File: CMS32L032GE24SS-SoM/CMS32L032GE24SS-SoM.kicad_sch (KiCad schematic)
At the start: 3 parts, among them J105 Connection to DAPLink Board

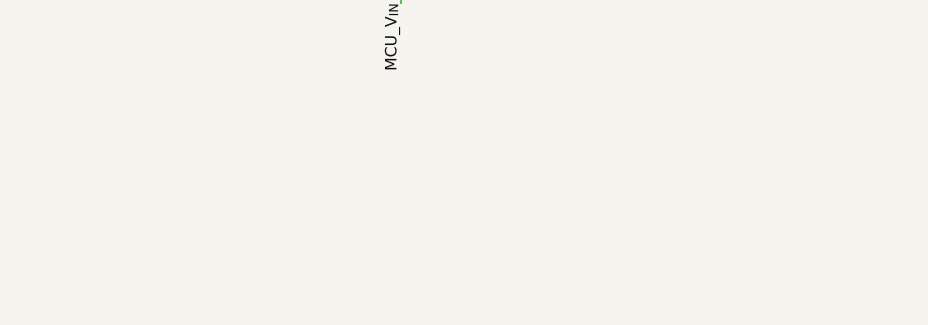
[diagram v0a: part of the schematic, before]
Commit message: basic layout of chips
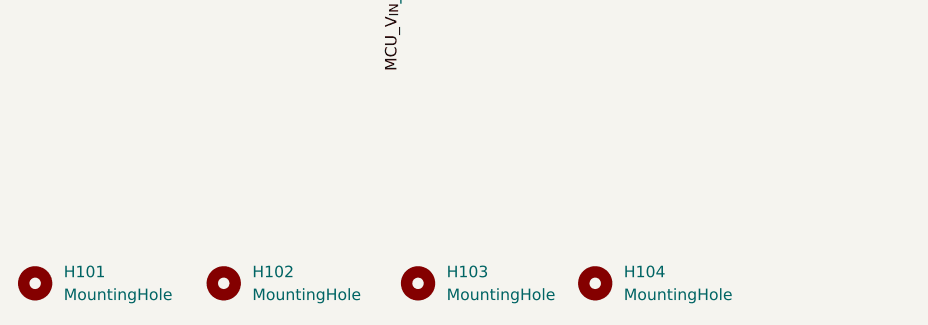
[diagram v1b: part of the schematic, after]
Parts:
- added H101, H102, H103, H104: MountingHole, IotPi_MountingHoles:MountingHole_1.8mm, symbol Mechanical:MountingHole
- J105: footprint (none) -> Connector_PinHeader_1.27mm:PinHeader_1x08_P1.27mm_Horizontal
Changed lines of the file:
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@@
     (effects (font (size 1.27 1.27)) (justify right bottom))
+  )
+  (symbol (lib_id "Mechanical:MountingHole") (at 86.995 183.515 0) (unit 1)
+    (in_bom no) (on_board yes) (dnp no) (fields_autoplaced)
+    (property "Reference" "H104" (at 90.17 182.245 0)
+      (effects (font (size 1.27 1.27)) (justify left))
+    )
+    (property "Value" "MountingHole" (at 90.17 184.785 0)
+      (effects (font (size 1.27 1.27)) (justify left))
+    )
+    (property "Footprint" "IotPi_MountingHoles:MountingHole_1.8mm" (at 86.995 183.515 0)
+      (effects (font (size 1.27 1.27)) hide)
+    )
+    (property "Datasheet" "~" (at 86.995 183.515 0)
+      (effects (font (size 1.27 1.27)) hide)
+    )
+    (instances
+      (project "CMS32L032GE24SS-SoM"
+        (path "/c0ebcd8e-c90a-40d9-842d-ee55e79d6adf"
+          (reference "H104") (unit 1)
+        )
+      )
+    )
+  )
+  (symbol (lib_id "Mechanical:MountingHole") (at 67.31 183.515 0) (unit 1)
+    (in_bom no) (on_board yes) (dnp no) (fields_autoplaced)
+    (property "Reference" "H103" (at 70.485 182.245 0)
+      (effects (font (size 1.27 1.27)) (justify left))
+    )
+    (property "Value" "MountingHole" (at 70.485 184.785 0)
+      (effects (font (size 1.27 1.27)) (justify left))
+    )
+    (property "Footprint" "IotPi_MountingHoles:MountingHole_1.8mm" (at 67.31 183.515 0)
+      (effects (font (size 1.27 1.27)) hide)
+    )
+    (property "Datasheet" "~" (at 67.31 183.515 0)
+      (effects (font (size 1.27 1.27)) hide)
+    )
+    (instances
+      (project "CMS32L032GE24SS-SoM"
+        (path "/c0ebcd8e-c90a-40d9-842d-ee55e79d6adf"
+          (reference "H103") (unit 1)
+        )
+      )
+    )
+  )
+  (symbol (lib_id "Mechanical:MountingHole") (at 24.765 183.515 0) (unit 1)
+    (in_bom no) (on_board yes) (dnp no) (fields_autoplaced)
+    (property "Reference" "H101" (at 27.94 182.245 0)
+      (effects (font (size 1.27 1.27)) (justify left))
+    )
+    (property "Value" "MountingHole" (at 27.94 184.785 0)
+      (effects (font (size 1.27 1.27)) (justify left))
+    )
+    (property "Footprint" "IotPi_MountingHoles:MountingHole_1.8mm" (at 24.765 183.515 0)
+      (effects (font (size 1.27 1.27)) hide)
+    )
+    (property "Datasheet" "~" (at 24.765 183.515 0)
+      (effects (font (size 1.27 1.27)) hide)
+    )
+    (instances
+      (project "CMS32L032GE24SS-SoM"
+        (path "/c0ebcd8e-c90a-40d9-842d-ee55e79d6adf"
+          (reference "H101") (unit 1)
+        )
+      )
+    )
   )
   (symbol (lib_id "power:PWR_FLAG") (at 83.82 110.49 0) (unit 1)
@@
         (path "/c0ebcd8e-c90a-40d9-842d-ee55e79d6adf"
           (reference "#PWR0103") (unit 1)
+        )
+      )
+    )
+  )
+  (symbol (lib_id "Mechanical:MountingHole") (at 45.72 183.515 0) (unit 1)
+    (in_bom no) (on_board yes) (dnp no) (fields_autoplaced)
+    (property "Reference" "H102" (at 48.895 182.245 0)
+      (effects (font (size 1.27 1.27)) (justify left))
+    )
+    (property "Value" "MountingHole" (at 48.895 184.785 0)
+      (effects (font (size 1.27 1.27)) (justify left))
+    )
+    (property "Footprint" "IotPi_MountingHoles:MountingHole_1.8mm" (at 45.72 183.515 0)
+      (effects (font (size 1.27 1.27)) hide)
+    )
+    (property "Datasheet" "~" (at 45.72 183.515 0)
+      (effects (font (size 1.27 1.27)) hide)
+    )
+    (instances
+      (project "CMS32L032GE24SS-SoM"
+        (path "/c0ebcd8e-c90a-40d9-842d-ee55e79d6adf"
+          (reference "H102") (unit 1)
         )
       )
@@
       (effects (font (size 1.27 1.27)))
     )
-    (property "Footprint" "" (at 41.91 34.925 0)
-      (effects (font (size 1.27 1.27)) hide)
-    )
+    (property "Footprint" "Connector_PinHeader_1.27mm:PinHeader_1x08_P1.27mm_Horizontal" (at 41.91 34.925 0)
+      (effects (font (size 1.27 1.27)) hide)
+    )

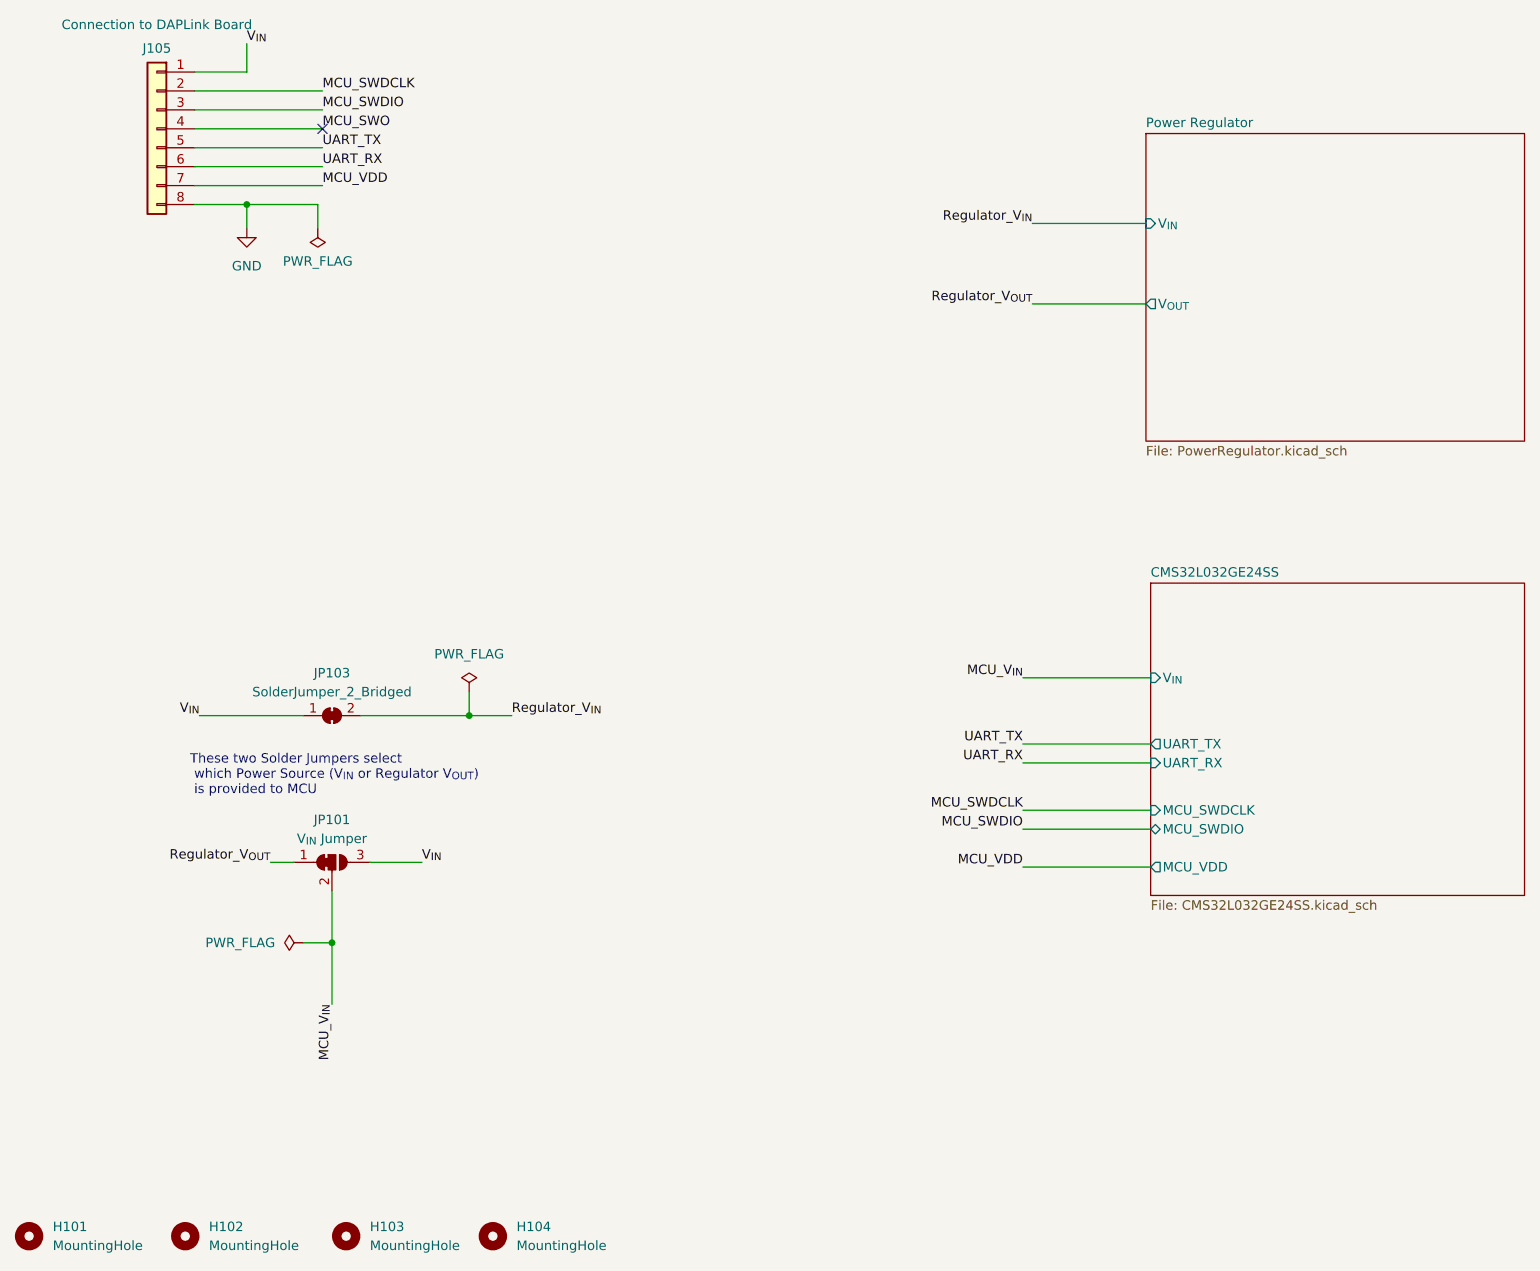
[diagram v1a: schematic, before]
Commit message: locked ArduinoNano board
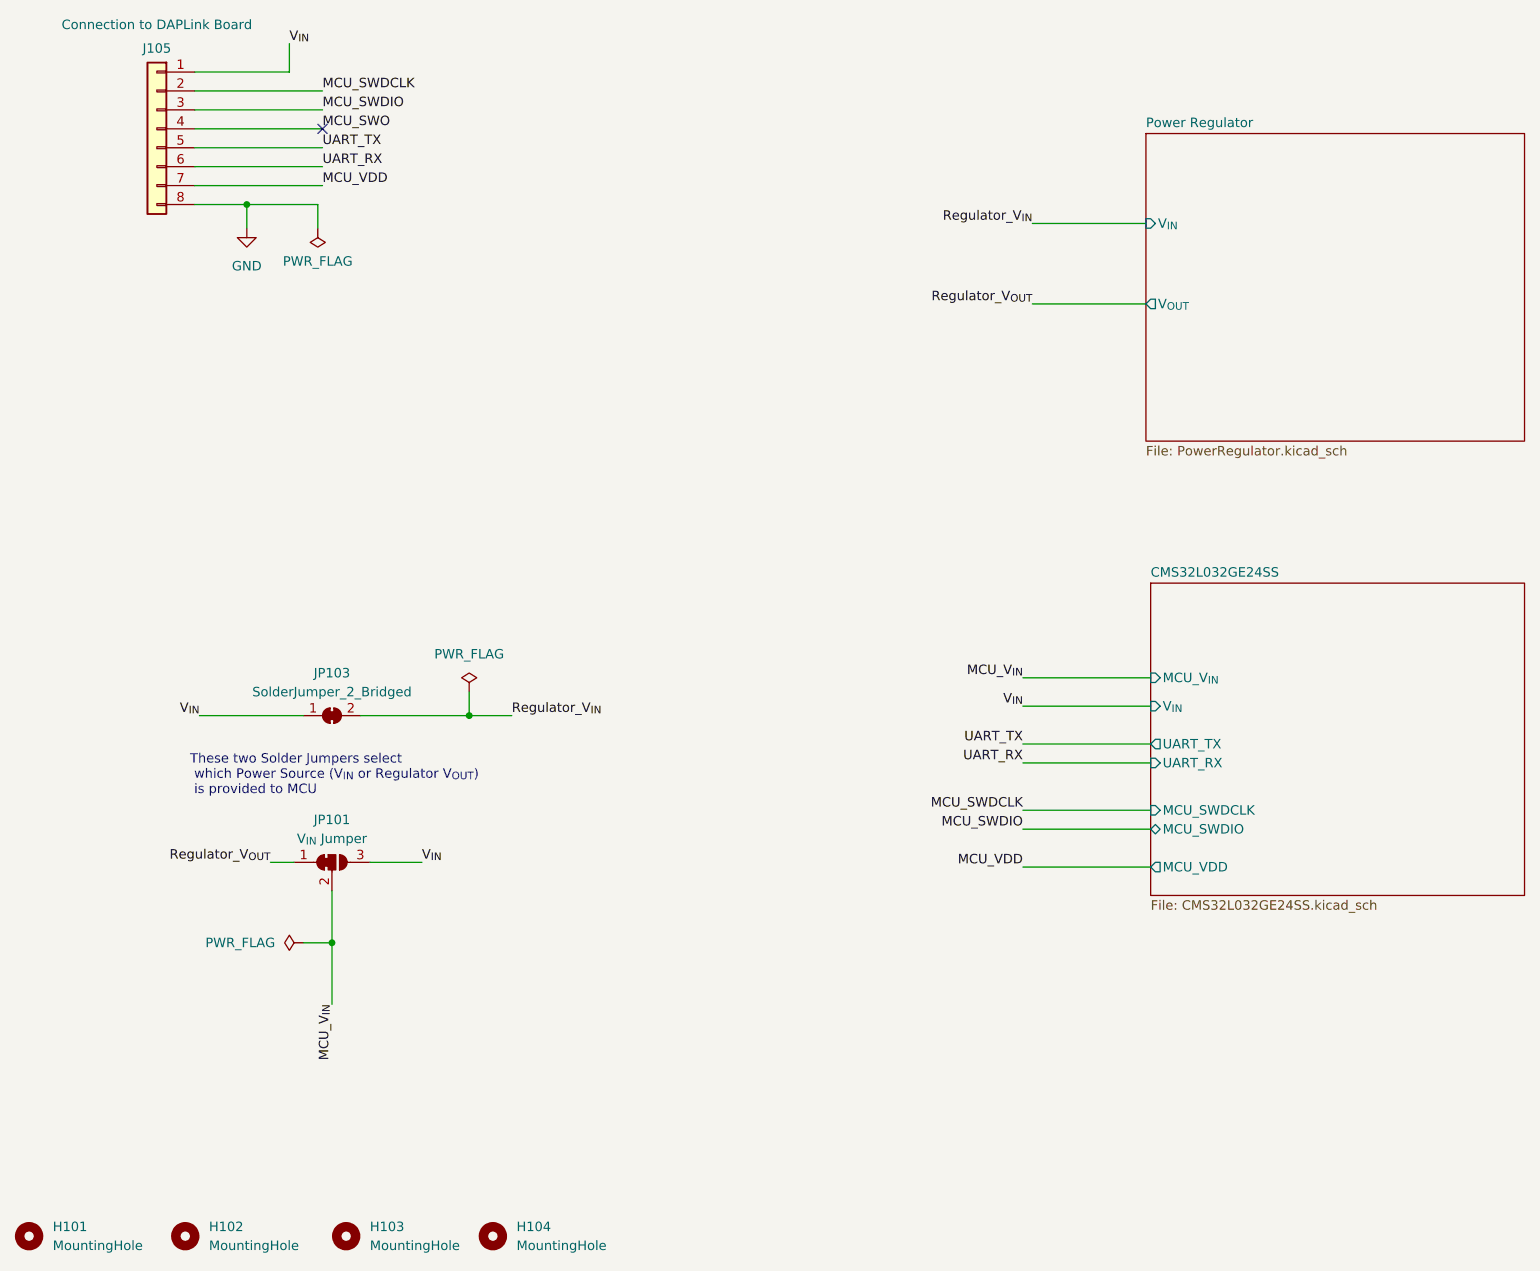
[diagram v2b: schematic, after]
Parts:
- H101, H102, H103, H104: footprint IotPi_MountingHoles:MountingHole_1.8mm -> IotPi_ArduinoNanoMountingHoles:ArduinoNano_MountingHole
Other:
- sheet CMS32L032GE24SS ports: added MCU_V_{IN}; removed none
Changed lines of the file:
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@@
     (stroke (width 0) (type default))
   )
-  (wire (pts (xy 53.975 27.305) (xy 46.99 27.305))
+  (wire (pts (xy 59.69 27.305) (xy 46.99 27.305))
     (stroke (width 0) (type default))
   )
@@
     (stroke (width 0) (type default))
   )
+  (wire (pts (xy 158.115 112.395) (xy 175.26 112.395))
+    (stroke (width 0) (type default))
+  )
   (wire (pts (xy 158.115 108.585) (xy 175.26 108.585))
     (stroke (width 0) (type default))
   )
-  (wire (pts (xy 53.975 23.495) (xy 53.975 27.305))
+  (wire (pts (xy 59.69 23.495) (xy 59.69 27.305))
     (stroke (width 0) (type default))
   )
@@
     (effects (font (size 1.27 1.27)) (justify left bottom))
   )
-  (label "V_{IN}" (at 53.975 23.495 0) (fields_autoplaced)
+  (label "V_{IN}" (at 59.69 23.495 0) (fields_autoplaced)
     (effects (font (size 1.27 1.27)) (justify left bottom))
   )
@@
   )
   (label "Regulator_V_{OUT}" (at 57.15 133.35 180) (fields_autoplaced)
+    (effects (font (size 1.27 1.27)) (justify right bottom))
+  )
+  (label "V_{IN}" (at 158.115 112.395 180) (fields_autoplaced)
     (effects (font (size 1.27 1.27)) (justify right bottom))
   )
@@
       (effects (font (size 1.27 1.27)) (justify left))
     )
-    (property "Footprint" "IotPi_MountingHoles:MountingHole_1.8mm" (at 86.995 183.515 0)
+    (property "Footprint" "IotPi_ArduinoNanoMountingHoles:ArduinoNano_MountingHole" (at 86.995 183.515 0)
       (effects (font (size 1.27 1.27)) hide)
     )
@@
       (effects (font (size 1.27 1.27)) (justify left))
     )
-    (property "Footprint" "IotPi_MountingHoles:MountingHole_1.8mm" (at 67.31 183.515 0)
+    (property "Footprint" "IotPi_ArduinoNanoMountingHoles:ArduinoNano_MountingHole" (at 67.31 183.515 0)
       (effects (font (size 1.27 1.27)) hide)
     )
@@
       (effects (font (size 1.27 1.27)) (justify left))
     )
-    (property "Footprint" "IotPi_MountingHoles:MountingHole_1.8mm" (at 24.765 183.515 0)
+    (property "Footprint" "IotPi_ArduinoNanoMountingHoles:ArduinoNano_MountingHole" (at 24.765 183.515 0)
       (effects (font (size 1.27 1.27)) hide)
     )
@@
       (effects (font (size 1.27 1.27)) (justify left))
     )
-    (property "Footprint" "IotPi_MountingHoles:MountingHole_1.8mm" (at 45.72 183.515 0)
+    (property "Footprint" "IotPi_ArduinoNanoMountingHoles:ArduinoNano_MountingHole" (at 45.72 183.515 0)
       (effects (font (size 1.27 1.27)) hide)
     )
@@
       (effects (font (size 1.27 1.27)) (justify left top))
     )
-    (pin "V_{IN}" input (at 175.26 108.585 180)
-      (effects (font (size 1.27 1.27)) (justify left))
-    )
     (pin "UART_TX" output (at 175.26 117.475 180)
       (effects (font (size 1.27 1.27)) (justify left))
@@
       (effects (font (size 1.27 1.27)) (justify left))
     )
+    (pin "MCU_V_{IN}" input (at 175.26 108.585 180)
+      (effects (font (size 1.27 1.27)) (justify left))
+    )
+    (pin "V_{IN}" input (at 175.26 112.395 180)
+      (effects (font (size 1.27 1.27)) (justify left))
+    )

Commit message: routing
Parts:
- J105: footprint Connector_PinHeader_1.27mm:PinHeader_1x08_P1.27mm_Horizontal -> Connector_PinHeader_1.27mm:PinHeader_1x08_P1.27mm_Vertical
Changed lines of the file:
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@@
       (effects (font (size 1.27 1.27)))
     )
-    (property "Footprint" "Connector_PinHeader_1.27mm:PinHeader_1x08_P1.27mm_Horizontal" (at 41.91 34.925 0)
+    (property "Footprint" "Connector_PinHeader_1.27mm:PinHeader_1x08_P1.27mm_Vertical" (at 41.91 34.925 0)
       (effects (font (size 1.27 1.27)) hide)
     )
